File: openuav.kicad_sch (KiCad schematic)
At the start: 62 parts, among them J1 Conn_01x01, J10 Conn_01x01, J11 Conn_01x01, J12 Conn_01x01, J13 Conn_01x01, J14 Conn_01x01, J15 Conn_01x01, J16 Conn_01x01, J17 Conn_01x01, J18 Conn_01x01, J19 Conn_01x01, J2 Conn_01x01, J20 Conn_01x01, J21 Conn_01x01, J22 Conn_01x01, J23 Conn_01x01, J24 Conn_01x01, J25 Conn_01x01, J26 Conn_01x01, J27 Conn_01x01, J28 Conn_01x01, J29 Conn_01x01, J3 Conn_01x01, J30 Conn_01x01, J31 Conn_01x01, J32 Conn_01x01, J4 Conn_01x01, J5 Conn_01x01, J6 Conn_01x01, J7 Conn_01x01, J8 Conn_01x01, J9 Conn_01x01, J99 USB_C_Receptacle_USB2.0, U1 STM32G431CBUx, U3 LSM6DSR, U4 LPS22HH, U5 TPS54202DDC, U6 W25N01GVZEIG, U7 XC6206P332MR

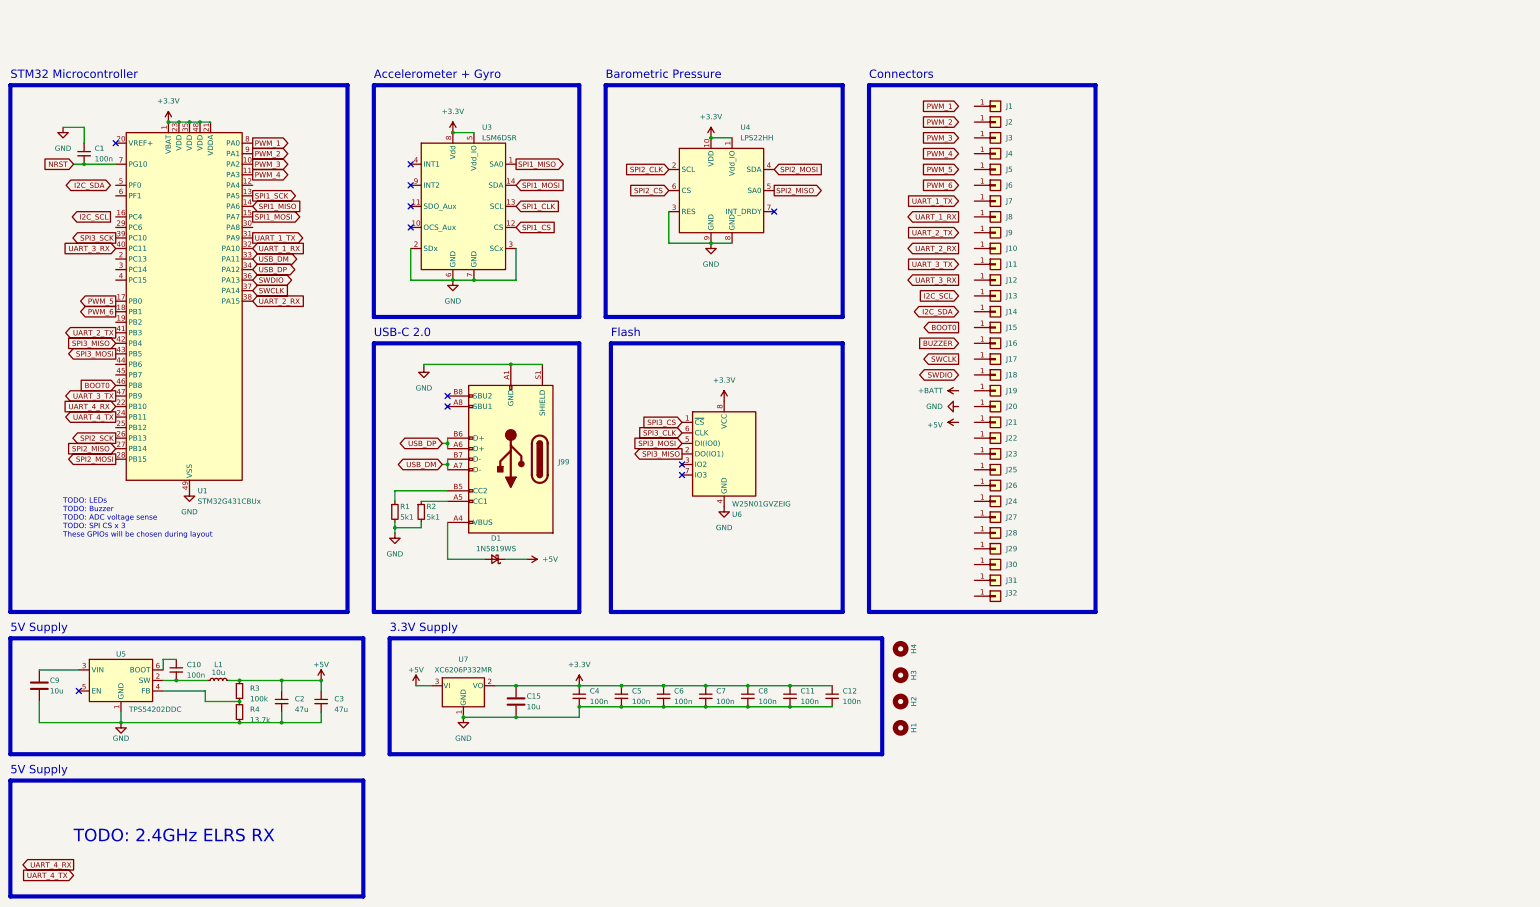
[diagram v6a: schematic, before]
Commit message: work on layout with JST-SH connectors
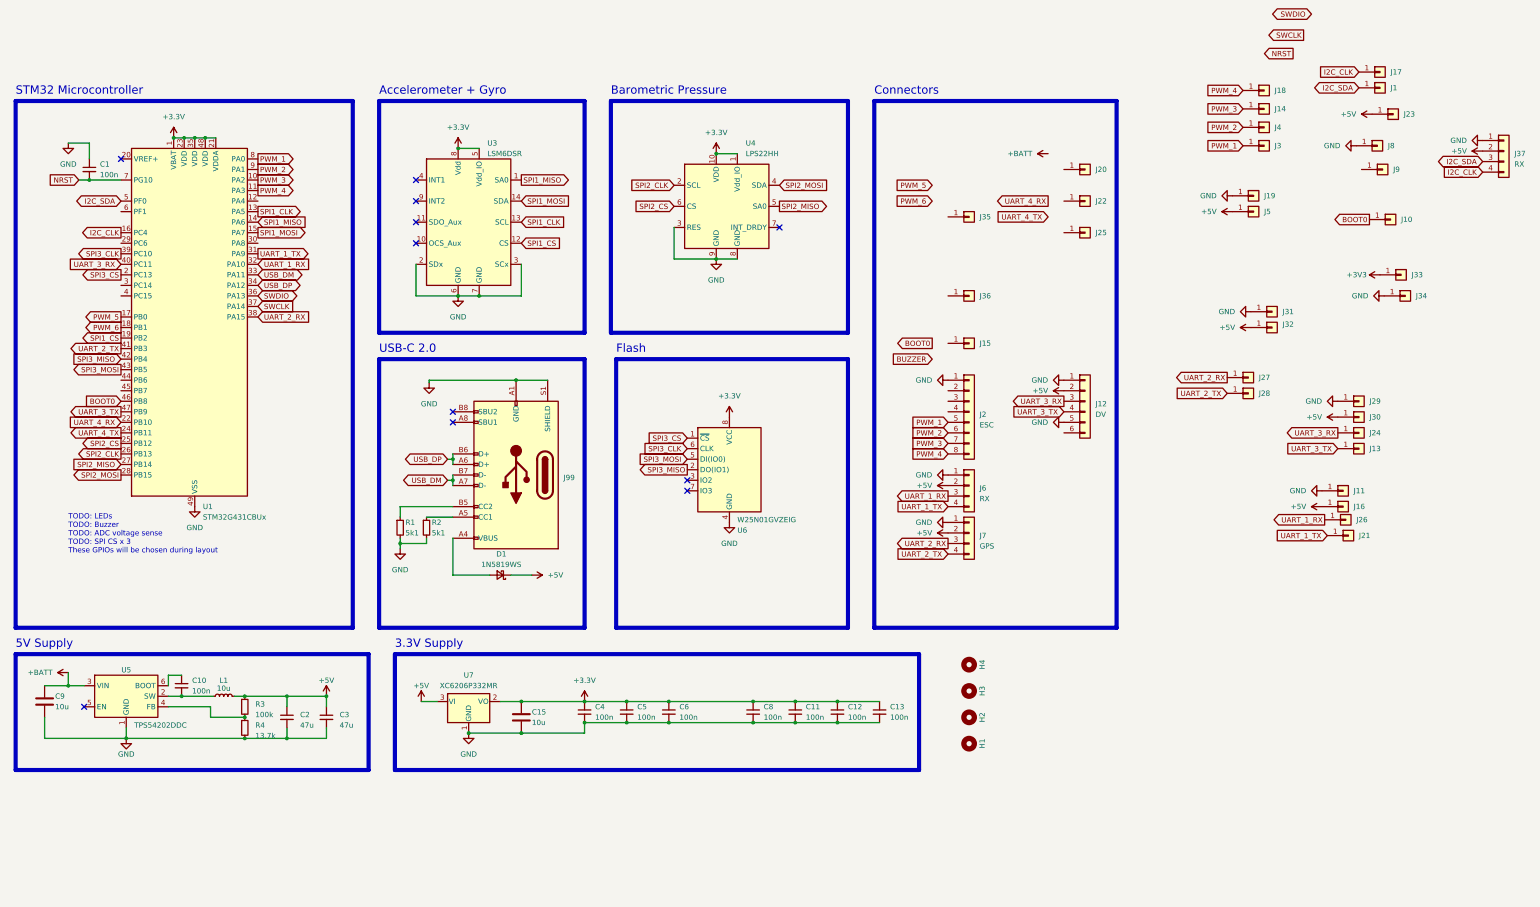
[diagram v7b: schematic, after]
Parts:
- removed C7: 100n, Capacitor_SMD:C_0402_1005Metric, symbol Device:C_Small
- removed J12, J2, J6, J7: Conn_01x01, Connector_Custom_Pads:TestPoint_Pad_2.0x3.0mm, symbol Connector_Generic:Conn_01x01
- added C13: 100n, Capacitor_SMD:C_0402_1005Metric, symbol Device:C_Small
- added J12: DV, Connector_JST:JST_SH_SM06B-SRSS-TB_1x06-1MP_P1.00mm_Horizontal, symbol Connector_Generic:Conn_01x06
- added J2: ESC, Connector_JST:JST_SH_SM08B-SRSS-TB_1x08-1MP_P1.00mm_Horizontal, symbol Connector_Generic:Conn_01x08
- added J33, J34, J35, J36: Conn_01x01, Connector_Custom_Pads:TestPoint_Pad_2.0x3.0mm, symbol Connector_Generic:Conn_01x01
- added J37, J6: RX, Connector_JST:JST_SH_SM04B-SRSS-TB_1x04-1MP_P1.00mm_Horizontal, symbol Connector_Generic:Conn_01x04
- added J7: GPS, Connector_JST:JST_SH_SM04B-SRSS-TB_1x04-1MP_P1.00mm_Horizontal, symbol Connector_Generic:Conn_01x04
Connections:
- net SPI1_SCK is gone; now on net SPI1_CLK: U1.13 (PA5)
- net SPI2_SCK is gone; now on net SPI2_CLK: U1.26 (PB13)
- net SPI3_SCK is gone; now on net SPI3_CLK: U1.39 (PC10)
- net +3V3: now also C13.1, J33.1 (Pin_1)
- net +5V: now also J16.1 (Pin_1), J23.1 (Pin_1), J30.1 (Pin_1), J32.1 (Pin_1), J5.1 (Pin_1), J12.2 (Pin_2), J37.2 (Pin_2), J6.2 (Pin_2), J7.2 (Pin_2)
- net +BATT: now also C9.1, U5.3 (VIN)
- net BOOT0: now also J10.1 (Pin_1)
- net GND: now also J11.1 (Pin_1), J19.1 (Pin_1), J29.1 (Pin_1), J31.1 (Pin_1), J8.1 (Pin_1), C13.2, J12.1 (Pin_1), J12.5 (Pin_5), J2.1 (Pin_1), J34.1 (Pin_1), J37.1 (Pin_1), J6.1 (Pin_1), J7.1 (Pin_1)
- net I2C_SDA: now also J1.1 (Pin_1), U1.5 (PF0), J37.3 (Pin_3)
- net PWM_1: now also J3.1 (Pin_1), J2.5 (Pin_5)
- net PWM_2: now also J4.1 (Pin_1), J2.6 (Pin_6)
- net PWM_3: now also J14.1 (Pin_1), J2.7 (Pin_7)
- net PWM_4: now also J18.1 (Pin_1), J2.8 (Pin_8)
- net SPI1_CS: now also U1.19 (PB2)
- net SPI2_CS: now also U1.25 (PB12)
- net SPI3_CS: now also U1.2 (PC13)
- net UART_1_RX: now also J26.1 (Pin_1), J6.3 (Pin_3)
- net UART_1_TX: now also J21.1 (Pin_1), J6.4 (Pin_4)
- net UART_2_RX: now also J27.1 (Pin_1), J7.3 (Pin_3)
- net UART_2_TX: now also J28.1 (Pin_1), J7.4 (Pin_4)
- net UART_3_RX: now also J24.1 (Pin_1), J12.3 (Pin_3)
- net UART_3_TX: now also J13.1 (Pin_1), J12.4 (Pin_4)
- net I2C_CLK: now reaches J17.1 (Pin_1)
- net I2C_CLK: now also U1.16 (PC4), J37.4 (Pin_4)
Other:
- note removed: "TODO: 2.4GHz ELRS RX"
- moved on the sheet: C1, C10, C11, C12, C15, C2, C3, C4, C5, C6, C8, C9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

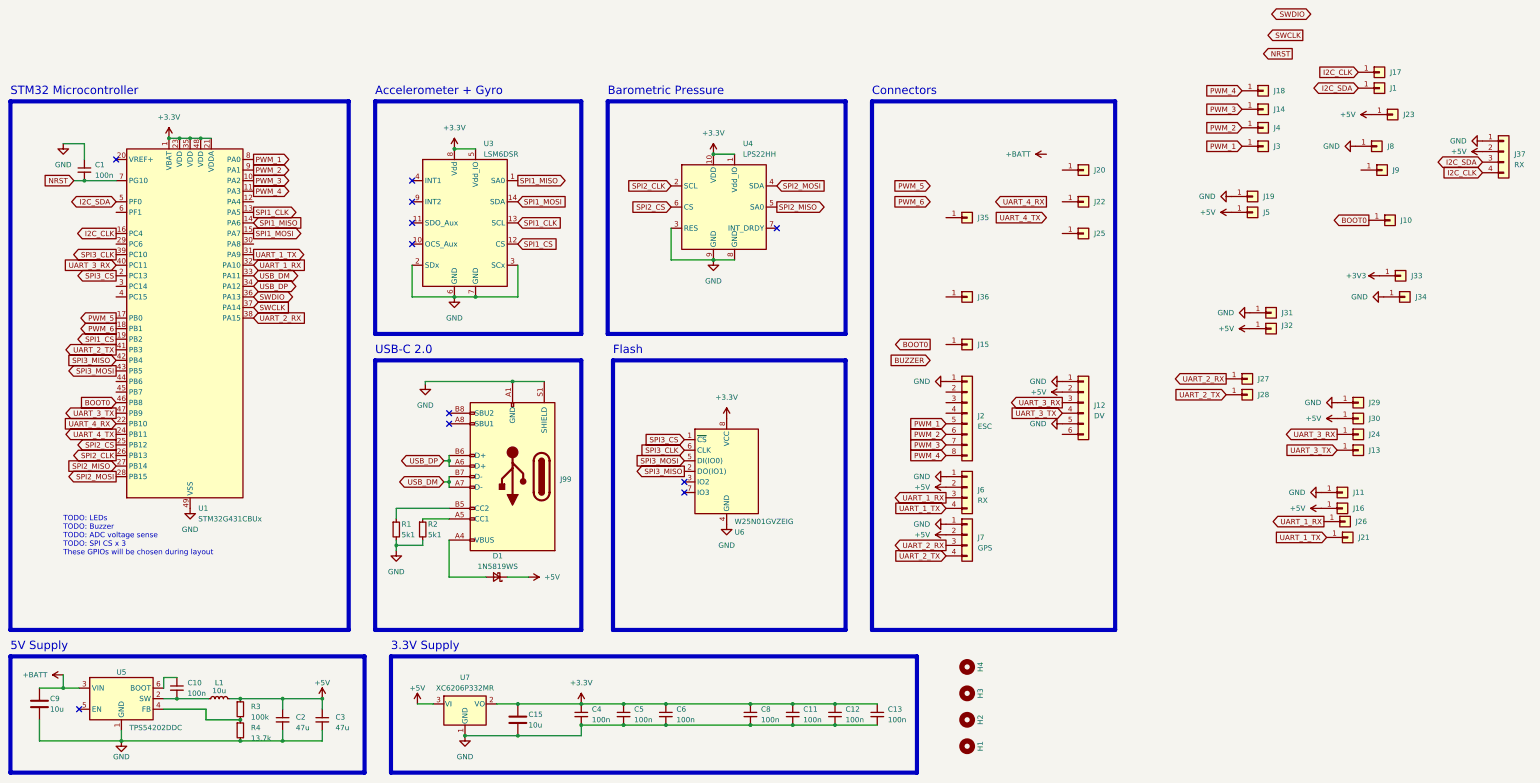
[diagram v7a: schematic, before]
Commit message: finish basic board layout
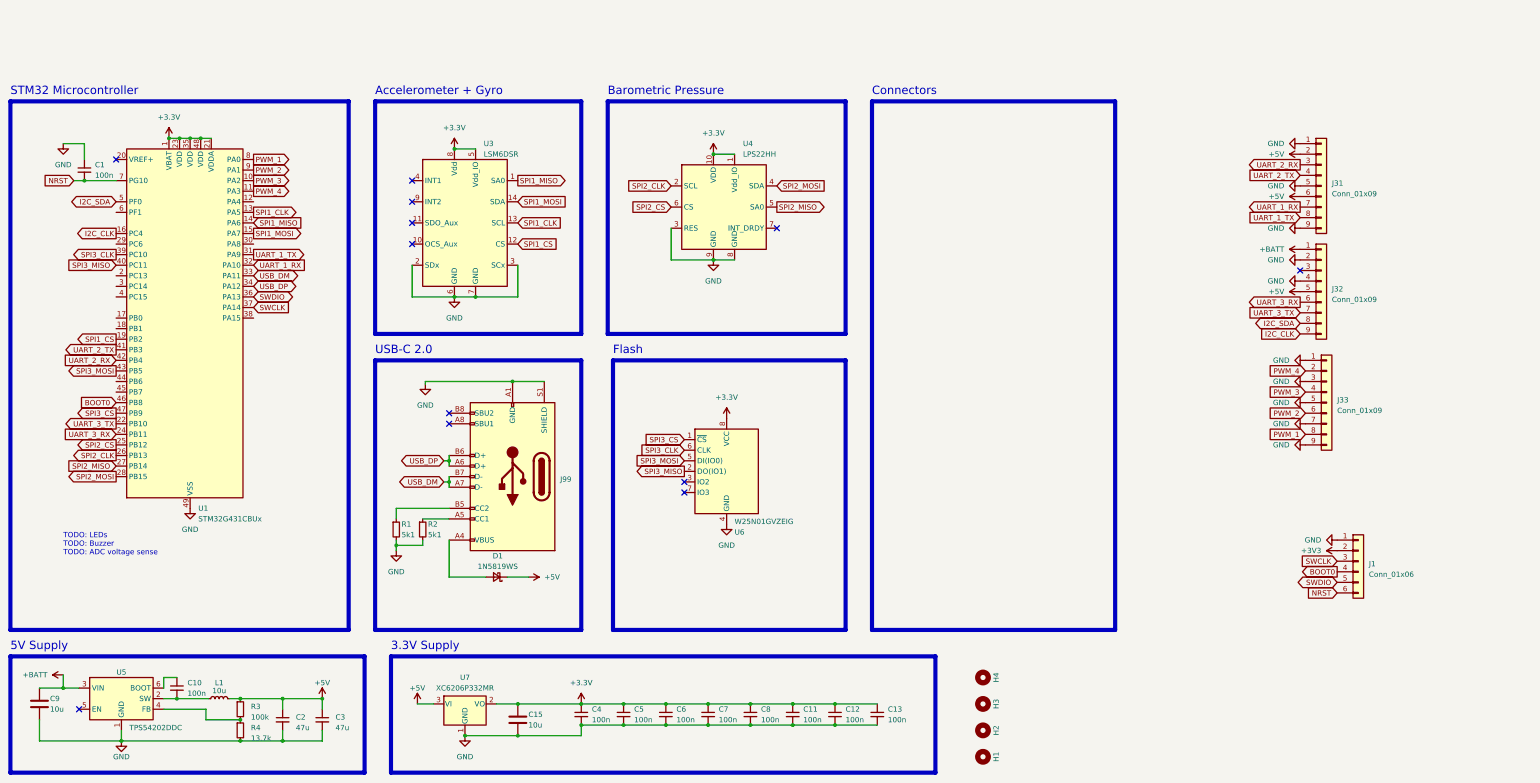
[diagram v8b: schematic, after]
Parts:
- removed J1, J10, J11, J13, J14, J15, J16, J17, J18, J19, J20, J21, J22, J23, J24, J25, J26, J27, J28, J29, J3, J30, J31, J32, J33, J34, J35, J36, J4, J5, J8, J9: Conn_01x01, Connector_Custom_Pads:TestPoint_Pad_2.0x3.0mm, symbol Connector_Generic:Conn_01x01
- removed J12: DV, Connector_JST:JST_SH_SM06B-SRSS-TB_1x06-1MP_P1.00mm_Horizontal, symbol Connector_Generic:Conn_01x06
- removed J2: ESC, Connector_JST:JST_SH_SM08B-SRSS-TB_1x08-1MP_P1.00mm_Horizontal, symbol Connector_Generic:Conn_01x08
- removed J37, J6: RX, Connector_JST:JST_SH_SM04B-SRSS-TB_1x04-1MP_P1.00mm_Horizontal, symbol Connector_Generic:Conn_01x04
- removed J7: GPS, Connector_JST:JST_SH_SM04B-SRSS-TB_1x04-1MP_P1.00mm_Horizontal, symbol Connector_Generic:Conn_01x04
- added C7: 100n, Capacitor_SMD:C_0402_1005Metric, symbol Device:C_Small
- added J1: Conn_01x06, Connector_PinHeader_2.54mm:PinHeader_2x03_P2.54mm_Vertical, symbol Connector_Generic:Conn_01x06
- added J31, J32, J33: Conn_01x09, Connector_PinHeader_2.54mm:PinHeader_1x09_P2.54mm_Vertical, symbol Connector_Generic:Conn_01x09
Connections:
- net UART_4_RX is gone; now on net UART_3_TX: U1.22 (PB10)
- net UART_4_TX is gone; now on net UART_3_RX: U1.24 (PB11)
- net +3V3: now also C7.1, J1.2 (Pin_2)
- net +5V: now also J31.2 (Pin_2), J31.6 (Pin_6), J32.5 (Pin_5)
- net +BATT: now also J32.1 (Pin_1)
- net BOOT0: now also J1.4 (Pin_4)
- net GND: now also C7.2, J1.1 (Pin_1), J31.1 (Pin_1), J31.5 (Pin_5), J31.9 (Pin_9), J32.2 (Pin_2), J32.4 (Pin_4), J33.1 (Pin_1), J33.3 (Pin_3), J33.5 (Pin_5), J33.7 (Pin_7), J33.9 (Pin_9)
- net I2C_CLK: now also J32.9 (Pin_9)
- net I2C_SDA: now also J32.8 (Pin_8)
- net NRST: now also J1.6 (Pin_6)
- net PWM_1: now also J33.8 (Pin_8)
- net PWM_2: now also J33.6 (Pin_6)
- net PWM_3: now also J33.4 (Pin_4)
- net PWM_4: now also J33.2 (Pin_2)
- net SPI3_CS: now also U1.47 (PB9); no longer U1.2 (PC13)
- net SPI3_MISO: now also U1.40 (PC11); no longer U1.42 (PB4)
- net SWCLK: now also J1.3 (Pin_3)
- net SWDIO: now also J1.5 (Pin_5)
- net UART_1_RX: now also J31.7 (Pin_7)
- net UART_1_TX: now also J31.8 (Pin_8)
- net UART_2_RX: now also U1.42 (PB4), J31.3 (Pin_3); no longer U1.38 (PA15)
- net UART_2_TX: now also J31.4 (Pin_4)
- net UART_3_RX: now also J32.6 (Pin_6); no longer U1.40 (PC11)
- net UART_3_TX: now also J32.7 (Pin_7); no longer U1.47 (PB9)
- net PWM_5: no longer names the net of U1.17 (PB0)
- net PWM_6: no longer names the net of U1.18 (PB1)
- no-connect marks 11 -> 12
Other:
- note added: "TODO: LEDs TODO: Buzzer TODO: ADC voltage sense"
- note removed: "TODO: LEDs TODO: Buzzer TODO: ADC voltage sense TODO: SPI CS x 3 These GPIOs will be chosen during layout"
- moved on the sheet: H1, H2, H3, H4
